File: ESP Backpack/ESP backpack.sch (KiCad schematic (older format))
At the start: 37 parts, among them J1 HLE-120-02-F-DV-BE-K, J2 HLE-120-02-F-DV-BE-K, U1 ESP32-DEVKITC-32D, U2 VCNL4010-GS08

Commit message: Re-org files for relative pathing, change extensions for globally unique names
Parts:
- 5VDC_IN1: symbol 282837-4:282837-4 -> ESP-backpack-rescue:282837-4-282837-4
- C10, C11, C12, C13, C14, C3, C4, C5, C6, C7, C8, C9: symbol EEE0JA102P:EEE0JA102P -> ESP-backpack-rescue:EEE0JA102P-EEE0JA102P
- D1: footprint LED_SK6812 -> Custom Libraries:LED_SK6812; symbol SK6812:SK6812 -> ESP-backpack-rescue:SK6812-SK6812
- J1, J2: symbol HLE-120-02-F-DV-BE-K:HLE-120-02-F-DV-BE-K -> ESP-backpack-rescue:HLE-120-02-F-DV-BE-K-HLE-120-02-F-DV-BE-K
- S1, S2: footprint 452403012014 -> Custom Libraries:452403012014; symbol 452403012014:452403012014 -> ESP-backpack-rescue:452403012014-452403012014
- U1: symbol ESP32-DEVKITC-32D:ESP32-DEVKITC-32D -> ESP-backpack-rescue:ESP32-DEVKITC-32D-ESP32-DEVKITC-32D
- U2: symbol VCNL4010-GS08:VCNL4010-GS08 -> ESP-backpack-rescue:VCNL4010-GS08-VCNL4010-GS08
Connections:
- wire segments 135 -> 136
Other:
- moved on the sheet: R10, R3, R4, R5, R6, R7

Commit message: edit all libs and footprints into single libraries and files. Issue fixes
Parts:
- removed 5VDC_IN1: 282837-4, Custom Libraries:TE_282837-4, symbol ESP-backpack-rescue:282837-4-282837-4
- removed C10, C11, C12, C13, C14, C3, C4, C5, C6, C7, C8, C9: EEE0JA102P, Custom Libraries:CAP_EEE0JA102P, symbol ESP-backpack-rescue:EEE0JA102P-EEE0JA102P
- added 5VDC_IN1: 282837-2, _ESP-Backpack-Custom-Libraries:TE_282837-2, symbol _esp-backpack-custom-schematic-library:282837-2
- added C10, C3, C4, C5, C6, C7, C8, C9: A765MU158M1ALAE014, _ESP-Backpack-Custom-Libraries:CAP_EEE0JA102P, symbol _esp-backpack-custom-schematic-library:A765MU158M1ALAE014
- D1: symbol ESP-backpack-rescue:SK6812-SK6812 -> _esp-backpack-custom-schematic-library:SK6812
- J1, J2: symbol ESP-backpack-rescue:HLE-120-02-F-DV-BE-K-HLE-120-02-F-DV-BE-K -> _esp-backpack-custom-schematic-library:HLE-120-02-F-DV-BE-K
- S1, S2: symbol ESP-backpack-rescue:452403012014-452403012014 -> _esp-backpack-custom-schematic-library:452403012014
- U1: symbol ESP-backpack-rescue:ESP32-DEVKITC-32D-ESP32-DEVKITC-32D -> _esp-backpack-custom-schematic-library:ESP32-DEVKITC-32D
- U2: symbol ESP-backpack-rescue:VCNL4010-GS08-VCNL4010-GS08 -> _esp-backpack-custom-schematic-library:VCNL4010-GS08
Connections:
- net +5V: now also 5VDC_IN1.2, C10.1, C3.1, C4.1, C5.1, C6.1, C7.1, C8.1, C9.1
- net GND: now also 5VDC_IN1.1, C10.2, C3.2, C4.2, C5.2, C6.2, C7.2, C8.2, C9.2

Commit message: reorg to more standard file tree
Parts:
- D1: footprint Custom Libraries:LED_SK6812 -> _ESP-Backpack-Custom-Libraries:LED_SK6812
- J1, J2: footprint Custom Libraries:SAMTEC_HLE-120-02-F-DV-BE-K -> _ESP-Backpack-Custom-Libraries:SAMTEC_HLE-120-02-F-DV-BE-K
- S1, S2: footprint Custom Libraries:452403012014 -> _ESP-Backpack-Custom-Libraries:452403012014
- U1: footprint Custom Libraries:MODULE_ESP32-DEVKITC-32D -> _ESP-Backpack-Custom-Libraries:MODULE_ESP32-DEVKITC-32D
- U2: footprint Custom Libraries:XDCR_VCNL4010-GS08 -> _ESP-Backpack-Custom-Libraries:XDCR_VCNL4010-GS08
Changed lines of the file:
@@
 F 0 "U2" H 7486 7320 50  0000 C CNN
 F 1 "VCNL4010-GS08" H 7486 7229 50  0000 C CNN
-F 2 "Custom Libraries:XDCR_VCNL4010-GS08" H 7550 6450 50  0001 L BNN
+F 2 "_ESP-Backpack-Custom-Libraries:XDCR_VCNL4010-GS08" H 7550 6450 50  0001 L BNN
 F 3 "" H 7550 6450 50  0001 L BNN
 F 4 "1.6" H 7550 6450 50  0001 L BNN "PARTREV"
@@
 F 0 "J1" H 3750 5967 50  0000 C CNN
 F 1 "HLE-120-02-F-DV-BE-K" H 3750 5876 50  0000 C CNN
-F 2 "Custom Libraries:SAMTEC_HLE-120-02-F-DV-BE-K" H 3750 4800 50  0001 L BNN
+F 2 "_ESP-Backpack-Custom-Libraries:SAMTEC_HLE-120-02-F-DV-BE-K" H 3750 4800 50  0001 L BNN
 F 3 "" H 3750 4800 50  0001 L BNN
 F 4 "SAMTEC" H 3750 4800 50  0001 L BNN "MANUFACTURER"
@@
 F 0 "J2" H 11750 5917 50  0000 C CNN
 F 1 "HLE-120-02-F-DV-BE-K" H 11750 5826 50  0000 C CNN
-F 2 "Custom Libraries:SAMTEC_HLE-120-02-F-DV-BE-K" H 11750 4750 50  0001 L BNN
+F 2 "_ESP-Backpack-Custom-Libraries:SAMTEC_HLE-120-02-F-DV-BE-K" H 11750 4750 50  0001 L BNN
 F 3 "" H 11750 4750 50  0001 L BNN
 F 4 "SAMTEC" H 11750 4750 50  0001 L BNN "MANUFACTURER"
@@
 F 0 "U1" H 7550 5067 50  0000 C CNN
 F 1 "ESP32-DEVKITC-32D" H 7550 4976 50  0000 C CNN
-F 2 "Custom Libraries:MODULE_ESP32-DEVKITC-32D" H 7550 3900 50  0001 L BNN
+F 2 "_ESP-Backpack-Custom-Libraries:MODULE_ESP32-DEVKITC-32D" H 7550 3900 50  0001 L BNN
 F 3 "" H 7550 3900 50  0001 L BNN
 F 4 "4" H 7550 3900 50  0001 L BNN "PARTREV"
@@
 F 0 "S1" H 9400 7117 50  0000 C CNN
 F 1 "452403012014" H 9400 7026 50  0000 C CNN
-F 2 "Custom Libraries:452403012014" H 9450 6600 50  0001 L BNN
+F 2 "_ESP-Backpack-Custom-Libraries:452403012014" H 9450 6600 50  0001 L BNN
 F 3 "" H 9450 6600 50  0001 L BNN
 	1    9450 6600
@@
 F 0 "D1" H 10350 3217 50  0000 C CNN
 F 1 "SK6812" H 10350 3126 50  0000 C CNN
-F 2 "Custom Libraries:LED_SK6812" H 10350 2750 50  0001 L BNN
+F 2 "_ESP-Backpack-Custom-Libraries:LED_SK6812" H 10350 2750 50  0001 L BNN
 F 3 "" H 10350 2750 50  0001 L BNN
 F 4 "Shenzhen LED Color" H 10350 2750 50  0001 L BNN "MANUFACTURER"
@@
 F 0 "S2" H 9400 8067 50  0000 C CNN
 F 1 "452403012014" H 9400 7976 50  0000 C CNN
-F 2 "Custom Libraries:452403012014" H 9450 7550 50  0001 L BNN
+F 2 "_ESP-Backpack-Custom-Libraries:452403012014" H 9450 7550 50  0001 L BNN
 F 3 "" H 9450 7550 50  0001 L BNN
 	1    9450 7550

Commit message: reorg into more traditional arrangement
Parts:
- 5VDC_IN1: symbol _esp-backpack-custom-schematic-library:282837-2 -> ESP-backpack-rescue:282837-2-_esp-backpack-custom-schematic-library
- C10, C3, C4, C5, C6, C7, C8, C9: symbol _esp-backpack-custom-schematic-library:A765MU158M1ALAE014 -> ESP-backpack-rescue:A765MU158M1ALAE014-_esp-backpack-custom-schematic-library
- D1: symbol _esp-backpack-custom-schematic-library:SK6812 -> ESP-backpack-rescue:SK6812-_esp-backpack-custom-schematic-library
- J1, J2: symbol _esp-backpack-custom-schematic-library:HLE-120-02-F-DV-BE-K -> ESP-backpack-rescue:HLE-120-02-F-DV-BE-K-_esp-backpack-custom-schematic-library
- S1, S2: symbol _esp-backpack-custom-schematic-library:452403012014 -> ESP-backpack-rescue:452403012014-_esp-backpack-custom-schematic-library
- U1: symbol _esp-backpack-custom-schematic-library:ESP32-DEVKITC-32D -> ESP-backpack-rescue:ESP32-DEVKITC-32D-_esp-backpack-custom-schematic-library
- U2: symbol _esp-backpack-custom-schematic-library:VCNL4010-GS08 -> ESP-backpack-rescue:VCNL4010-GS08-_esp-backpack-custom-schematic-library
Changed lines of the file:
@@
 $EndComp
 $Comp
-L _esp-backpack-custom-schematic-library:VCNL4010-GS08 U2
+L ESP-backpack-rescue:VCNL4010-GS08-_esp-backpack-custom-schematic-library U2
 U 1 1 6158E28C
 P 7550 6450
@@
 $EndComp
 $Comp
-L _esp-backpack-custom-schematic-library:HLE-120-02-F-DV-BE-K J1
+L ESP-backpack-rescue:HLE-120-02-F-DV-BE-K-_esp-backpack-custom-schematic-library J1
 U 1 1 6162485D
 P 3750 4800
@@
 $EndComp
 $Comp
-L _esp-backpack-custom-schematic-library:HLE-120-02-F-DV-BE-K J2
+L ESP-backpack-rescue:HLE-120-02-F-DV-BE-K-_esp-backpack-custom-schematic-library J2
 U 1 1 61621D28
 P 11750 4750
@@
 $EndComp
 $Comp
-L _esp-backpack-custom-schematic-library:ESP32-DEVKITC-32D U1
+L ESP-backpack-rescue:ESP32-DEVKITC-32D-_esp-backpack-custom-schematic-library U1
 U 1 1 61592B24
 P 7550 3900
@@
 	12350 5250 12250 5250
 $Comp
-L _esp-backpack-custom-schematic-library:452403012014 S1
+L ESP-backpack-rescue:452403012014-_esp-backpack-custom-schematic-library S1
 U 1 1 616D4E57
 P 9450 6600
@@
 $EndComp
 $Comp
-L _esp-backpack-custom-schematic-library:SK6812 D1
+L ESP-backpack-rescue:SK6812-_esp-backpack-custom-schematic-library D1
 U 1 1 616D71C8
 P 10350 2750
@@
 $EndComp
 $Comp
-L _esp-backpack-custom-schematic-library:452403012014 S2
+L ESP-backpack-rescue:452403012014-_esp-backpack-custom-schematic-library S2
 U 1 1 616D852D
 P 9450 7550
@@
 	7550 1150 7850 1150
 $Comp
-L _esp-backpack-custom-schematic-library:A765MU158M1ALAE014 C3
+L ESP-backpack-rescue:A765MU158M1ALAE014-_esp-backpack-custom-schematic-library C3
 U 1 1 61C67DBE
 P 7950 1250
@@
 	7850 1450 8150 1450
 $Comp
-L _esp-backpack-custom-schematic-library:A765MU158M1ALAE014 C4
+L ESP-backpack-rescue:A765MU158M1ALAE014-_esp-backpack-custom-schematic-library C4
 U 1 1 61C71FFD
 P 8250 1250
@@
 	8150 1450 8450 1450
 $Comp
-L _esp-backpack-custom-schematic-library:A765MU158M1ALAE014 C5
+L ESP-backpack-rescue:A765MU158M1ALAE014-_esp-backpack-custom-schematic-library C5
 U 1 1 61C72568
 P 8550 1250
@@
 	8450 1450 8750 1450
 $Comp
-L _esp-backpack-custom-schematic-library:A765MU158M1ALAE014 C6
+L ESP-backpack-rescue:A765MU158M1ALAE014-_esp-backpack-custom-schematic-library C6
 U 1 1 61C72A87
 P 8850 1250
@@
 	8750 1450 9050 1450
 $Comp
-L _esp-backpack-custom-schematic-library:A765MU158M1ALAE014 C7
+L ESP-backpack-rescue:A765MU158M1ALAE014-_esp-backpack-custom-schematic-library C7
 U 1 1 61C72C92
 P 9150 1250
@@
 	9050 1450 9350 1450
 $Comp
-L _esp-backpack-custom-schematic-library:A765MU158M1ALAE014 C8
+L ESP-backpack-rescue:A765MU158M1ALAE014-_esp-backpack-custom-schematic-library C8
 U 1 1 61C730DF
 P 9450 1250
@@
 	9350 1450 9650 1450
 $Comp
-L _esp-backpack-custom-schematic-library:A765MU158M1ALAE014 C9
+L ESP-backpack-rescue:A765MU158M1ALAE014-_esp-backpack-custom-schematic-library C9
 U 1 1 61C738BA
 P 9750 1250
@@
 	9650 1450 9950 1450
 $Comp
-L _esp-backpack-custom-schematic-library:A765MU158M1ALAE014 C10
+L ESP-backpack-rescue:A765MU158M1ALAE014-_esp-backpack-custom-schematic-library C10
 U 1 1 61C73CBB
 P 10050 1250
@@
 $EndComp
 $Comp
-L _esp-backpack-custom-schematic-library:282837-2 5VDC_IN1
+L ESP-backpack-rescue:282837-2-_esp-backpack-custom-schematic-library 5VDC_IN1
 U 1 1 61C99002
 P 7600 8850

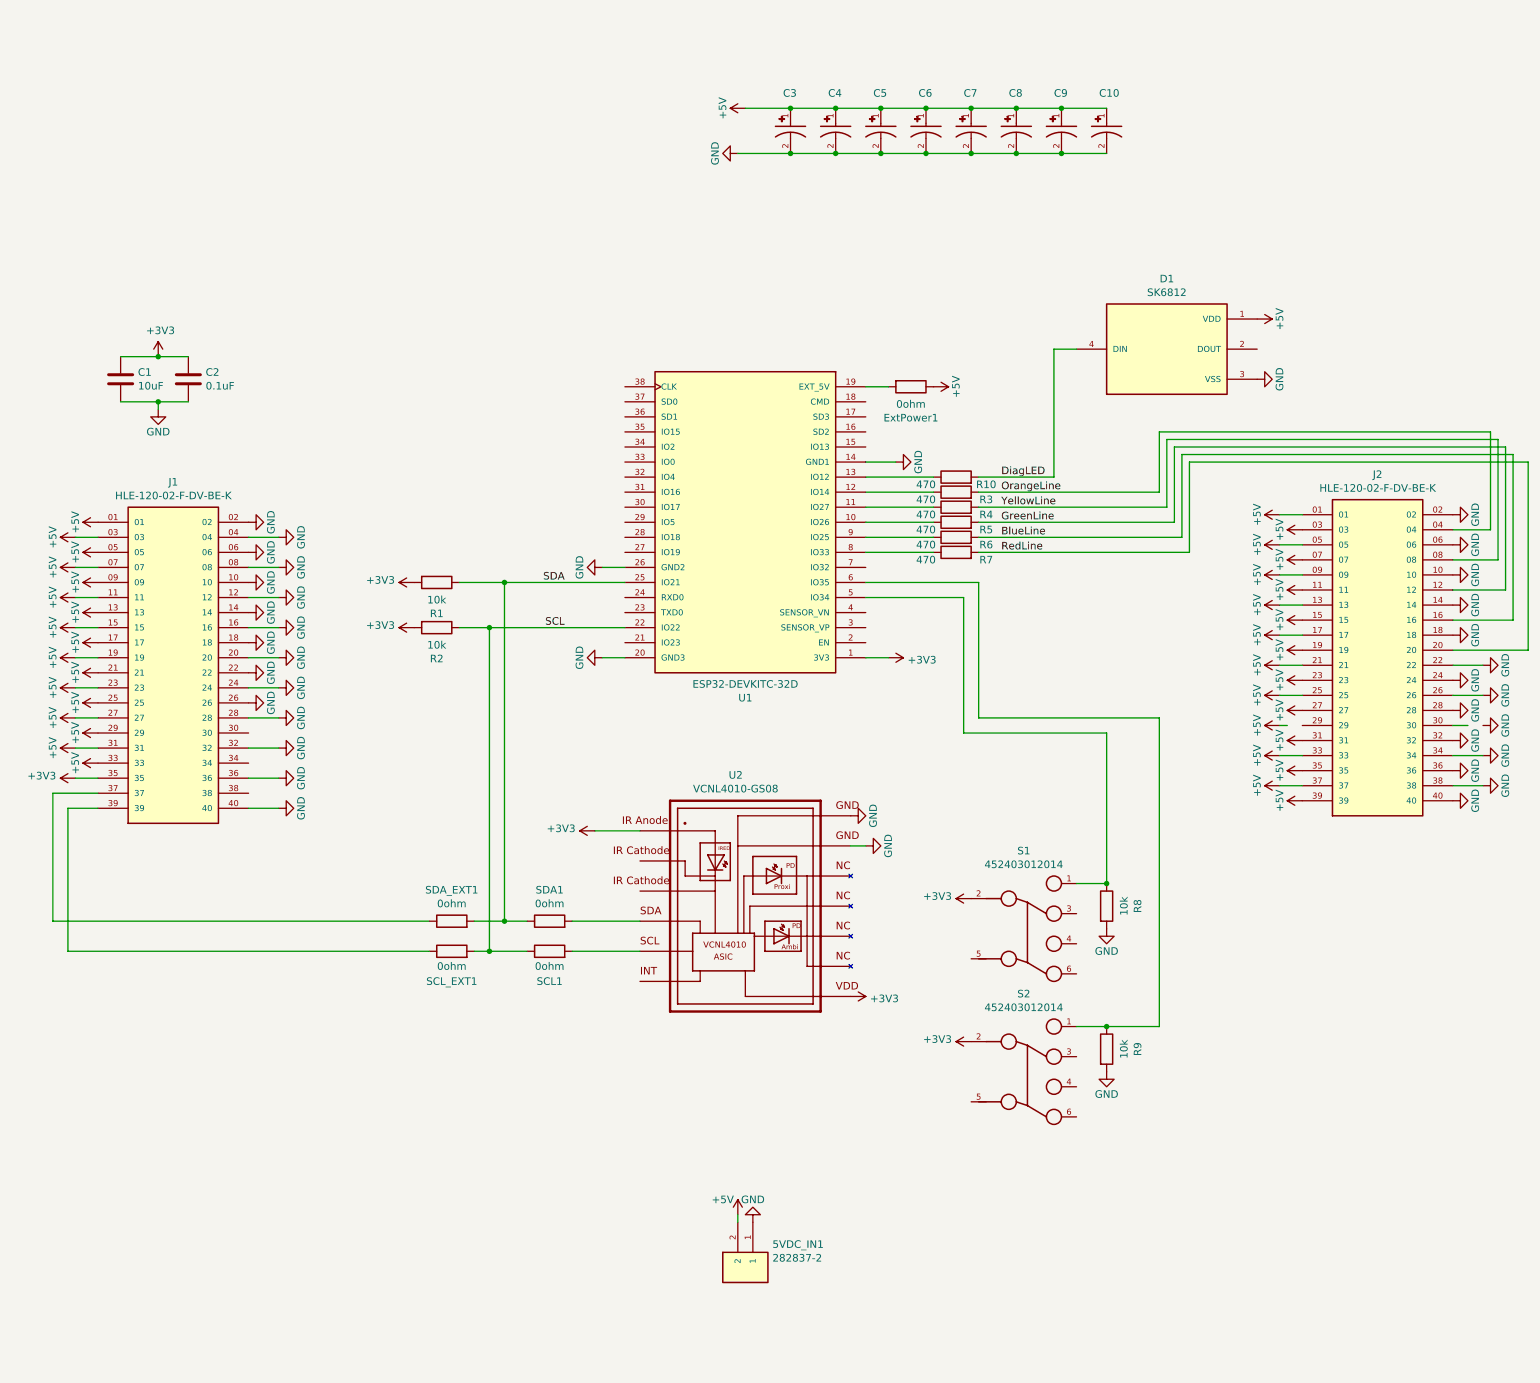
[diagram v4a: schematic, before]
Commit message: fixes #17, #18, #15 and adds RTC
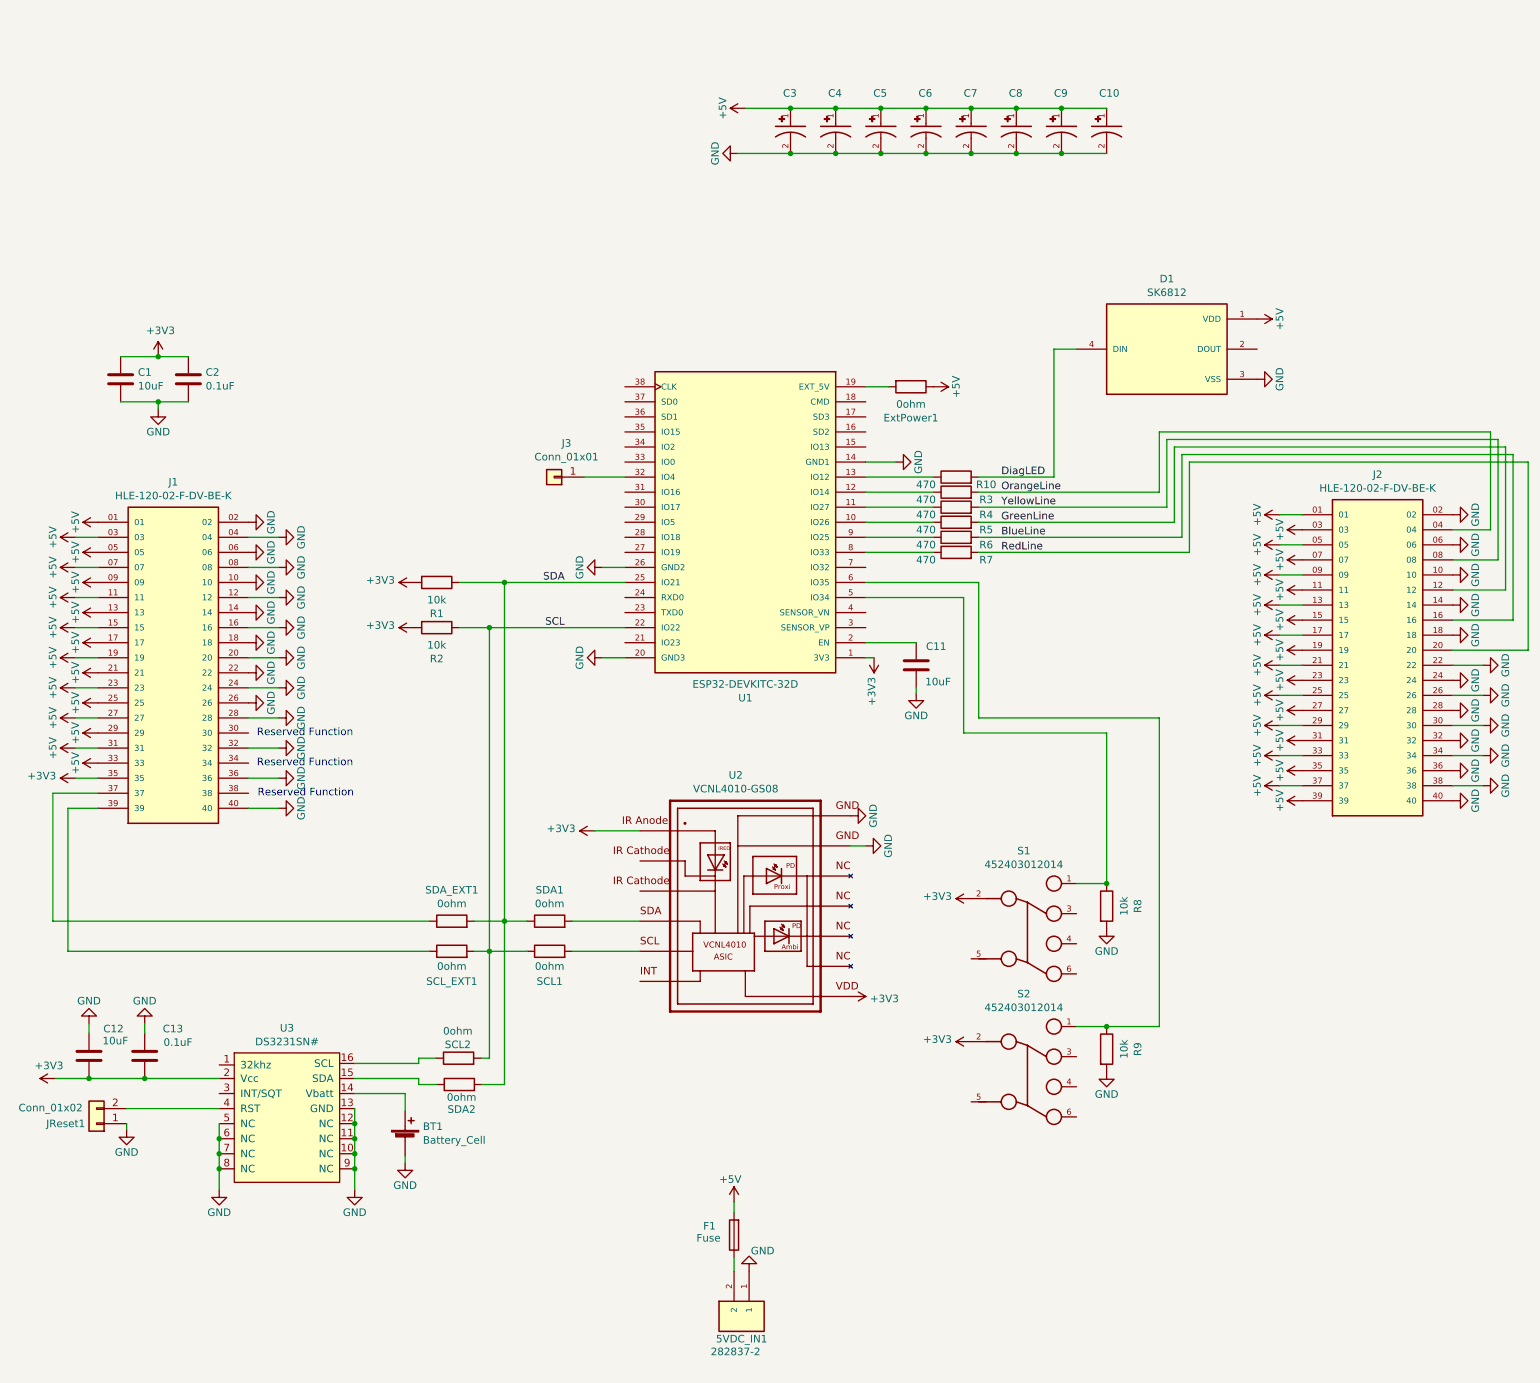
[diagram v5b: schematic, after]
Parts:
- added BT1: Battery_Cell, _ESP-Backpack-Custom-Libraries:Keystone_2894, symbol Device:Battery_Cell
- added C11, C12: 10uF, Capacitor_SMD:C_0603_1608Metric, symbol Device:C
- added C13: 0.1uF, Capacitor_SMD:C_0603_1608Metric, symbol Device:C
- added F1: Fuse, _ESP-Backpack-Custom-Libraries:Keystone-3658, symbol Device:Fuse
- added J3: Conn_01x01, Connector_PinHeader_2.54mm:PinHeader_1x01_P2.54mm_Vertical, symbol Connector_Generic:Conn_01x01
- added JReset1: Conn_01x02, Connector_PinHeader_2.54mm:PinHeader_1x02_P2.54mm_Vertical, symbol Connector_Generic:Conn_01x02
- added SCL2, SDA2: 0ohm, Resistor_SMD:R_0603_1608Metric, symbol Device:R
- added U3: DS3231SN#, Package_SO:SOIC-16W_7.5x10.3mm_P1.27mm, symbol _esp-backpack-custom-schematic-library:DS3231SN#
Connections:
- net +3V3: now also C12.2, C13.2, U3.2 (Vcc)
- net +5V: now also J2.29, F1.2; no longer 5VDC_IN1.2
- net GND: now also J2.30, BT1.2 (-), C11.2, C12.1, C13.1, JReset1.1 (Pin_1), U3.10 (NC), U3.11 (NC), U3.12 (NC), U3.13 (GND), U3.5 (NC), U3.6 (NC), U3.7 (NC), U3.8 (NC), U3.9 (NC)
- net SCL: now also SCL2.2
- net SDA: now also SDA2.2
- net at U1.2 (EN): now also C11.1
- net at U1.32 (IO4): now also J3.1 (Pin_1)
- new net: 5VDC_IN1.2, F1.1
- new net: BT1.1 (+), U3.14 (Vbatt)
- new net: SDA2.1, U3.15 (SDA)
- new net: SCL2.1, U3.16 (SCL)
- new net: JReset1.2 (Pin_2), U3.4 (RST)
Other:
- note added: "Reserved Function"
- moved on the sheet: 5VDC_IN1
